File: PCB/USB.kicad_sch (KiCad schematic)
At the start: 9 parts, among them J2 USB, U5 TUSB321

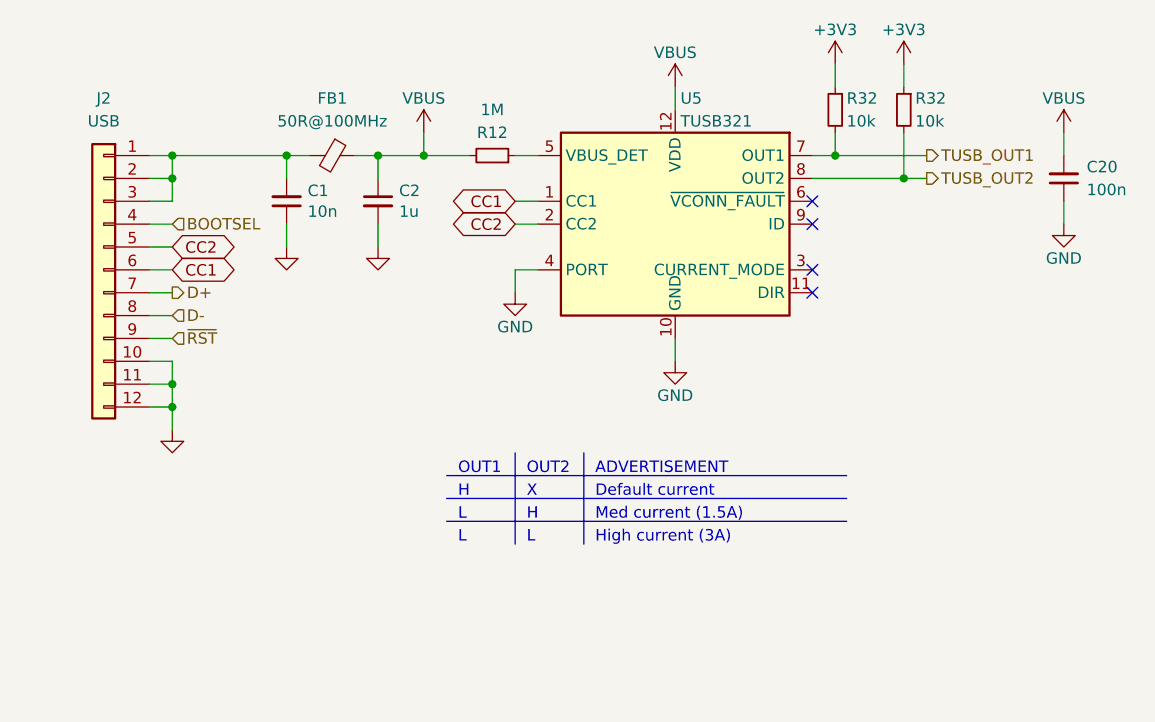
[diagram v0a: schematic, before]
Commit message: 14/07/2023 update
Replaced 1N4148 switch diodes with BAV70. Replaced switch footprints with combination MX/Choc hotswap footprints. Replaced flash IC with much smaller version. Removed buttons and USB-C port and replaced it with an FFC connector for [Galia](https://github.com/Ariamelon/Galia) (a USB-C daughterboard designed specifically for the Honeydew). Added case STEP file and renders.
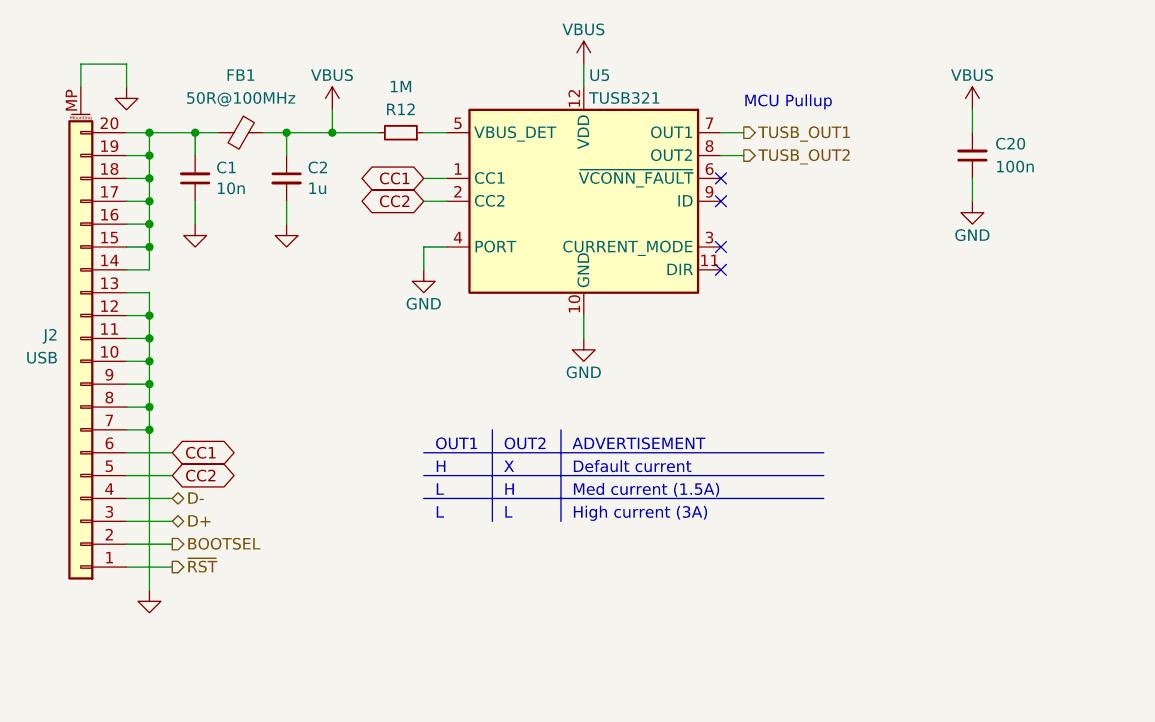
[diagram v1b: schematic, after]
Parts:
- removed J2: USB, Connector_FFC-FPC:TE_1-84953-2_1x12-1MP_P1.0mm_Horizontal, symbol Connector_Generic:Conn_01x12
- removed R32 (x2): 10k, Resistor_SMD:R_0402_1005Metric, symbol Device:R_Small
- added J2: USB, Honeydew:HRS_FH34SRJ-20S-0.5SH(50), symbol Connector_Generic_MountingPin:Conn_01x20_MountingPin
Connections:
- net BOOTSEL: now also J2.2 (Pin_2)
- net CC1: now also J2.6 (Pin_6)
- net CC2: now also J2.5 (Pin_5)
- net D+: now also J2.3 (Pin_3)
- net D-: now also J2.4 (Pin_4)
- net GND: now also J2.10 (Pin_10), J2.11 (Pin_11), J2.12 (Pin_12), J2.13 (Pin_13), J2.7 (Pin_7), J2.8 (Pin_8), J2.9 (Pin_9), J2.MP (MountPin)
- net ~{RST}: now also J2.1 (Pin_1)
- net at C1.2, FB1.2: now also J2.14 (Pin_14), J2.15 (Pin_15), J2.16 (Pin_16), J2.17 (Pin_17), J2.18 (Pin_18), J2.19 (Pin_19), J2.20 (Pin_20)
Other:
- note added: "MCU Pullup"
- moved on the sheet: C1, C2, C20, FB1, R12, U5

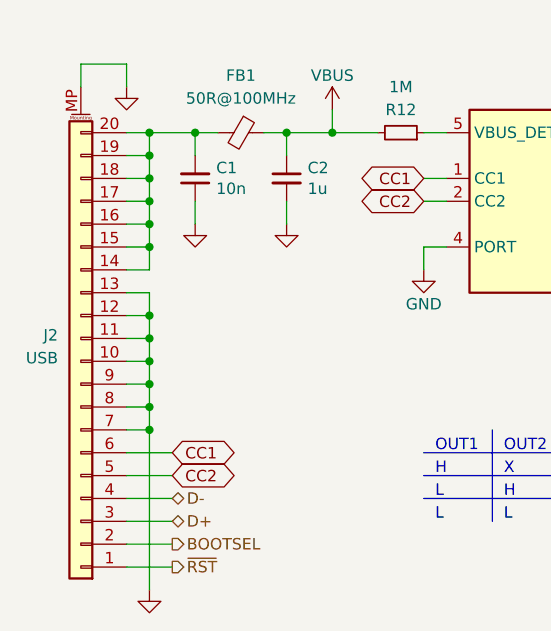
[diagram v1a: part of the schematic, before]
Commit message: 17/07/2023 update
Changed 20 pin FFC connector to 14 pin JST SH connector. Repositioned components.
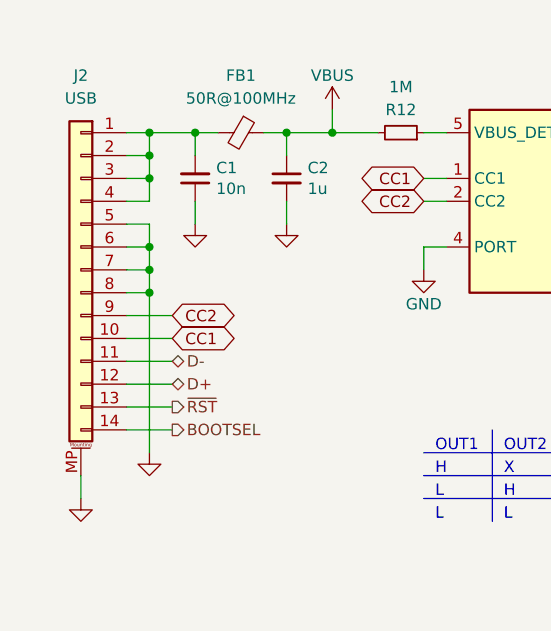
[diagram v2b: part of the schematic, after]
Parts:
- removed J2: USB, Honeydew:HRS_FH34SRJ-20S-0.5SH(50), symbol Connector_Generic_MountingPin:Conn_01x20_MountingPin
- added J2: USB, Honeydew:JST_SH_SM14B-SRSS-TB_1x14-1MP_P1.00mm_Horizontal, symbol Connector_Generic_MountingPin:Conn_01x14_MountingPin
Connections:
- net BOOTSEL: now also J2.14 (Pin_14)
- net CC1: now also J2.10 (Pin_10)
- net CC2: now also J2.9 (Pin_9)
- net D+: now also J2.12 (Pin_12)
- net D-: now also J2.11 (Pin_11)
- net GND: now also J2.5 (Pin_5), J2.6 (Pin_6), J2.7 (Pin_7), J2.8 (Pin_8), J2.MP (MountPin)
- net ~{RST}: now also J2.13 (Pin_13)
- net at C1.2, FB1.2: now also J2.1 (Pin_1), J2.2 (Pin_2), J2.3 (Pin_3), J2.4 (Pin_4)

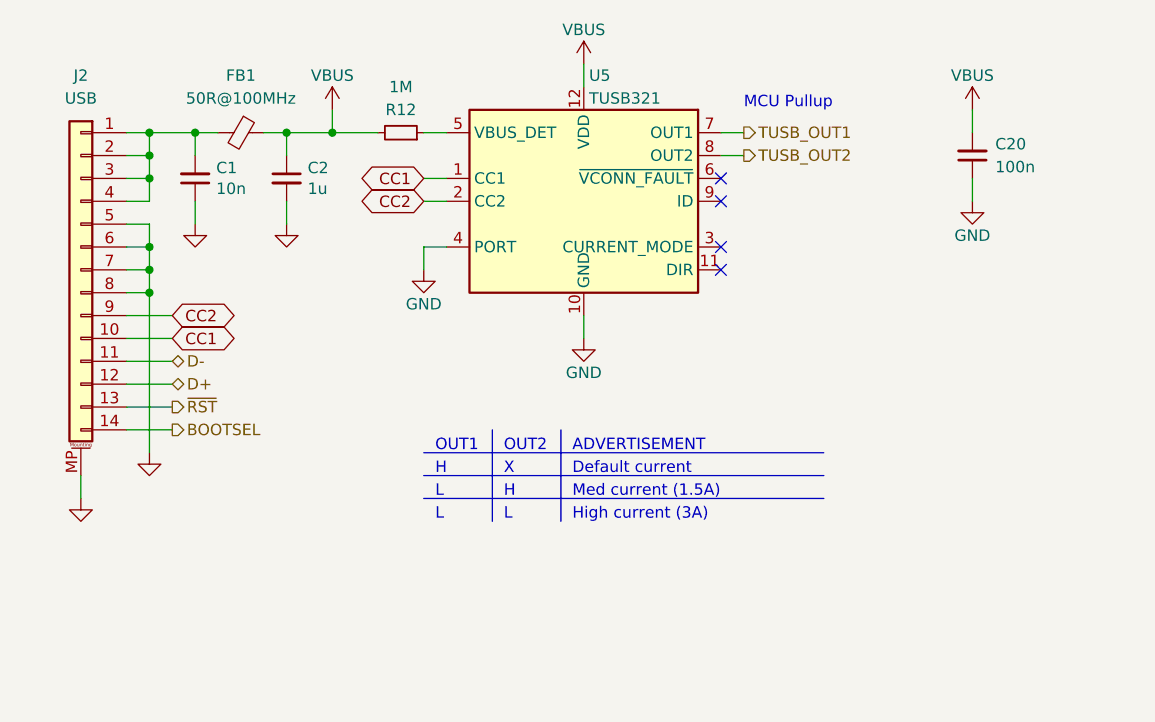
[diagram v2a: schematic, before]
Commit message: 18/07/2023 update.
Changed JST connector back to 20 pin FFC. Centered connector. Increased size of PMW3360 cutout.
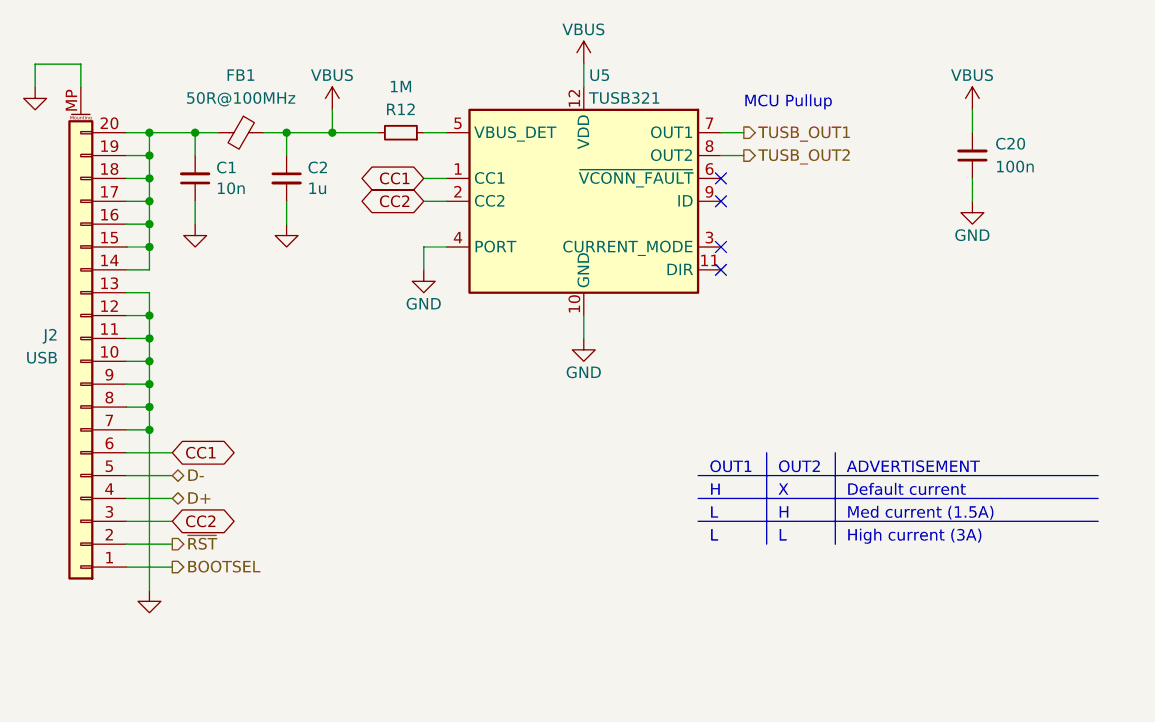
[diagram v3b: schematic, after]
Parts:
- removed J2: USB, Honeydew:JST_SH_SM14B-SRSS-TB_1x14-1MP_P1.00mm_Horizontal, symbol Connector_Generic_MountingPin:Conn_01x14_MountingPin
- added J2: USB, Honeydew:HRS_FH34SRJ-20S-0.5SH(50), symbol Connector_Generic_MountingPin:Conn_01x20_MountingPin
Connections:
- net BOOTSEL: now also J2.1 (Pin_1)
- net CC1: now also J2.6 (Pin_6)
- net CC2: now also J2.3 (Pin_3)
- net D+: now also J2.4 (Pin_4)
- net D-: now also J2.5 (Pin_5)
- net GND: now also J2.10 (Pin_10), J2.11 (Pin_11), J2.12 (Pin_12), J2.13 (Pin_13), J2.7 (Pin_7), J2.8 (Pin_8), J2.9 (Pin_9), J2.MP (MountPin)
- net ~{RST}: now also J2.2 (Pin_2)
- net at C1.2, FB1.2: now also J2.14 (Pin_14), J2.15 (Pin_15), J2.16 (Pin_16), J2.17 (Pin_17), J2.18 (Pin_18), J2.19 (Pin_19), J2.20 (Pin_20)

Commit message: 21/07/2023 update.
Fixed routing. Changed 20 pin FFC to 7 pin and 8 pin JST SH connector.
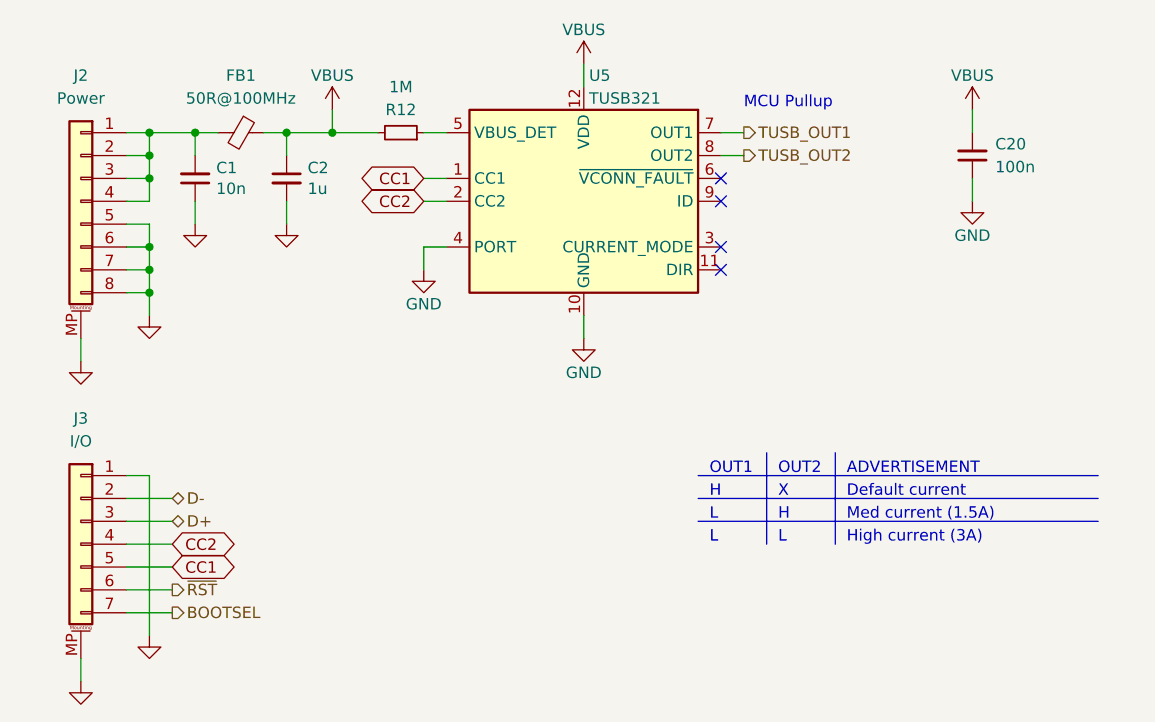
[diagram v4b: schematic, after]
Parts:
- removed J2: USB, Honeydew:HRS_FH34SRJ-20S-0.5SH(50), symbol Connector_Generic_MountingPin:Conn_01x20_MountingPin
- added J2: Power, Honeydew:JST_SH_SM08B-SRSS-TB_1x08-1MP_P1.00mm_Horizontal, symbol Connector_Generic_MountingPin:Conn_01x08_MountingPin
- added J3: I/O, Honeydew:JST_SH_SM07B-SRSS-TB_1x07-1MP_P1.00mm_Horizontal, symbol Connector_Generic_MountingPin:Conn_01x07_MountingPin
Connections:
- net BOOTSEL: now also J3.7 (Pin_7)
- net CC1: now also J3.5 (Pin_5)
- net CC2: now also J3.4 (Pin_4)
- net D+: now also J3.3 (Pin_3)
- net D-: now also J3.2 (Pin_2)
- net GND: now also J2.5 (Pin_5), J2.6 (Pin_6), J2.7 (Pin_7), J2.8 (Pin_8), J2.MP (MountPin), J3.1 (Pin_1), J3.MP (MountPin)
- net ~{RST}: now also J3.6 (Pin_6)
- net at C1.2, FB1.2: now also J2.1 (Pin_1), J2.2 (Pin_2), J2.3 (Pin_3), J2.4 (Pin_4)
